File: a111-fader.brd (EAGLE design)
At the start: 100 x 50 mm, 50 parts, among them U1 FADER-KNOB-8MM(BLACK/WHITE), U10 NUT-M2-SELFLOCK, U11 FX2-20S-1.27DS, U12 ERM1-5MM, U2 SCREW-M2X8, U3 SCREW-M2X8, U4 NUT-M2-SELFLOCK, U5 NUT-M2-SELFLOCK, U6 FX2-20P-1.27DS, U7 SCREW-M2X8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

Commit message: A111 New VU Indicator preliminary
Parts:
- removed DA2: LM2903N, ic-fairchild:DIP-8
- removed R13: 22K(TH), resistors:R-0207/10
- removed R15: 100R(TH), resistors:R-0207/10
- added DA3: TL072IP, ic-ti:DIP-8
- added R20, R21: 100K(TH), resistors:R-0207/10
- added R22: 15K(TH), resistors:R-0207/10
- added R23: 470K(TH), resistors:R-0207/10
- HL1: value RED/BLUE(2MMX5MM,CC) -> RED/GREEN(2MMX5MM,CC)
- R19: value 4K7(TH) -> 10K(TH)
- R24: value 1K8(TH) -> 300K(TH)
- R25: value 10K(TH) -> 1K(TH)
- R26: value 2K2(TH) -> 1K(TH)
- R6, R8: value 10M(TH) -> 1M(TH)
- R7, R9: value 100K(TH) -> 33K(TH)
- moved C7 3.00 mm to (21.0, 39.0)
- moved C8 3.00 mm to (35.0, 39.0)
- turned R24 to 90 degrees
- renumbered R14 to R19, R16 to R25, R17 to R26, R18 to R24
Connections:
- removed net N$26: DA2.2, R15.2, R19.1
- removed net N$27: DA2.6, R13.1, R19.2
- removed net N$28: DA2.1, HL1.A2, R24.1, VT1.1
- removed net N$45: C1.+, C3.2, C7.2, DA1.8, DA2.8, L1.2
- removed net N$47: C2.-, C4.1, C8.1, DA1.4, DA2.4, L2.2
- removed net N$48: DA2.7, HL1.A1, R25.2, R26.1
- removed net N$49: R25.1, VT1.2
- new net N$13: DA3.6, R19.2, R20.1
- new net N$17: DA3.7, R20.2, R26.1
- new net N$29: HL1.A2, R26.2, VT1.1
- new net N$30: DA3.2, R21.1, R22.2, R23.2
- new net N$31: DA3.1, R21.2, R24.1, R25.1
- new net N$32: R24.2, VT1.2
- new net N$33: HL1.A1, R25.2
- net +15V: now also C1.+, C3.2, C7.2, DA1.8, DA3.8, L1.2, R23.1; no longer R13.2
- net -15V: now also C2.-, C4.1, C8.1, DA1.4, DA3.4, L2.2; no longer HL1.K, VT1.3
- net GND: now also HL1.K, R19.1, R22.1, VT1.3; no longer R15.1, R24.2, R26.2
- net N$24: now also DA3.3, DA3.5; no longer DA2.3, DA2.5
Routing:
- net N$45: track 112.4 -> 0.00 mm
- net N$47: track 92.3 -> 0.00 mm
- net N$26: track 44.5 -> 0.00 mm
- net N$24: track 61.0 -> 22.9 mm
- net -15V: track 5.96 -> 43.3 mm
- net N$27: track 33.1 -> 0.00 mm
- net N$28: track 19.8 -> 0.00 mm
- net N$48: track 18.2 -> 0.00 mm
- net N$49: track 4.07 -> 0.00 mm
- net +15V: track 44.9 -> 43.1 mm

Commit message: A111a Routing
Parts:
- removed R24: 300K(TH), resistors:R-0207/10
- removed R25: 1K(TH), resistors:R-0207/10
- added R13: 10K(TH), resistors:R-0207/10
- added R16: 100K(TH), resistors:R-0207/10
- R19: value 10K(TH) -> 1K(TH)
- R20: value 100K(TH) -> 300K(TH)
- moved R19 26.6 mm to (13.0, 40.0), turned to 90 degrees
- moved R20 22.5 mm to (5.00, 37.0), turned to 90 degrees
- renumbered DA3 to DA2, R21 to R17, R22 to R15, R23 to R14, R26 to R18
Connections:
- net GND: now also R13.1; no longer R19.1
- net N$13: now also R13.2, R16.1; no longer R19.2, R20.1
- net N$17: now also R16.2; no longer R20.2
- net N$31: now also R19.1, R20.1; no longer R24.1, R25.1
- net N$32: now also R20.2; no longer R24.2
- net N$33: now also R19.2; no longer R25.2
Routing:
- net +15V: track 43.1 -> 157.5 mm, vias 0 -> 1
- net -15V: track 43.3 -> 103.2 mm, vias 0 -> 1
- net N$30: track 0.00 -> 52.0 mm
- net N$13: track 0.00 -> 31.4 mm
- net N$24: track 22.9 -> 53.3 mm
- net N$31: track 0.00 -> 23.5 mm
- net N$17: track 0.00 -> 14.6 mm
- net N$32: track 0.00 -> 10.9 mm
- net N$29: track 0.00 -> 8.74 mm
- net N$33: track 0.00 -> 4.16 mm

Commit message: A111a: Resistor Value Update
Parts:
- R20: value 300K(TH) -> 330K(TH)
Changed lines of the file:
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@@
 <element name="R15" library="resistors" package="R-0207/10" value="15K(TH)" x="22" y="7" rot="R180"/>
 <element name="R14" library="resistors" package="R-0207/10" value="470K(TH)" x="19" y="40" rot="R90"/>
-<element name="R20" library="resistors" package="R-0207/10" value="300K(TH)" x="5" y="37" rot="R90"/>
+<element name="R20" library="resistors" package="R-0207/10" value="330K(TH)" x="5" y="37" rot="R90"/>
 <element name="R19" library="resistors" package="R-0207/10" value="1K(TH)" x="13" y="40" rot="R90">
 <attribute name="MOUSER" value="71-RN55D-F-1.0K" x="13" y="40" size="1.778" layer="27" rot="R90" display="off"/>

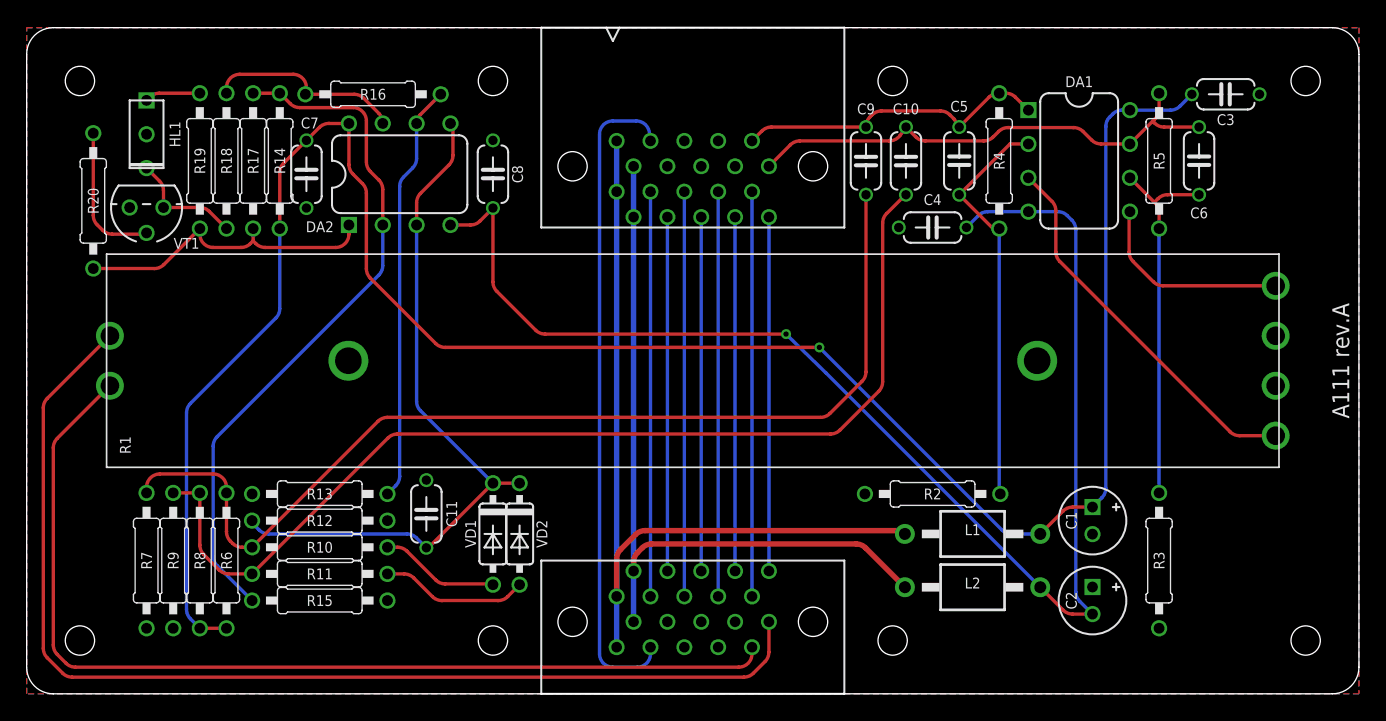
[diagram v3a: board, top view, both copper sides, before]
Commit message: A111 Change resistor positioning to better tolerate 0207 resistors
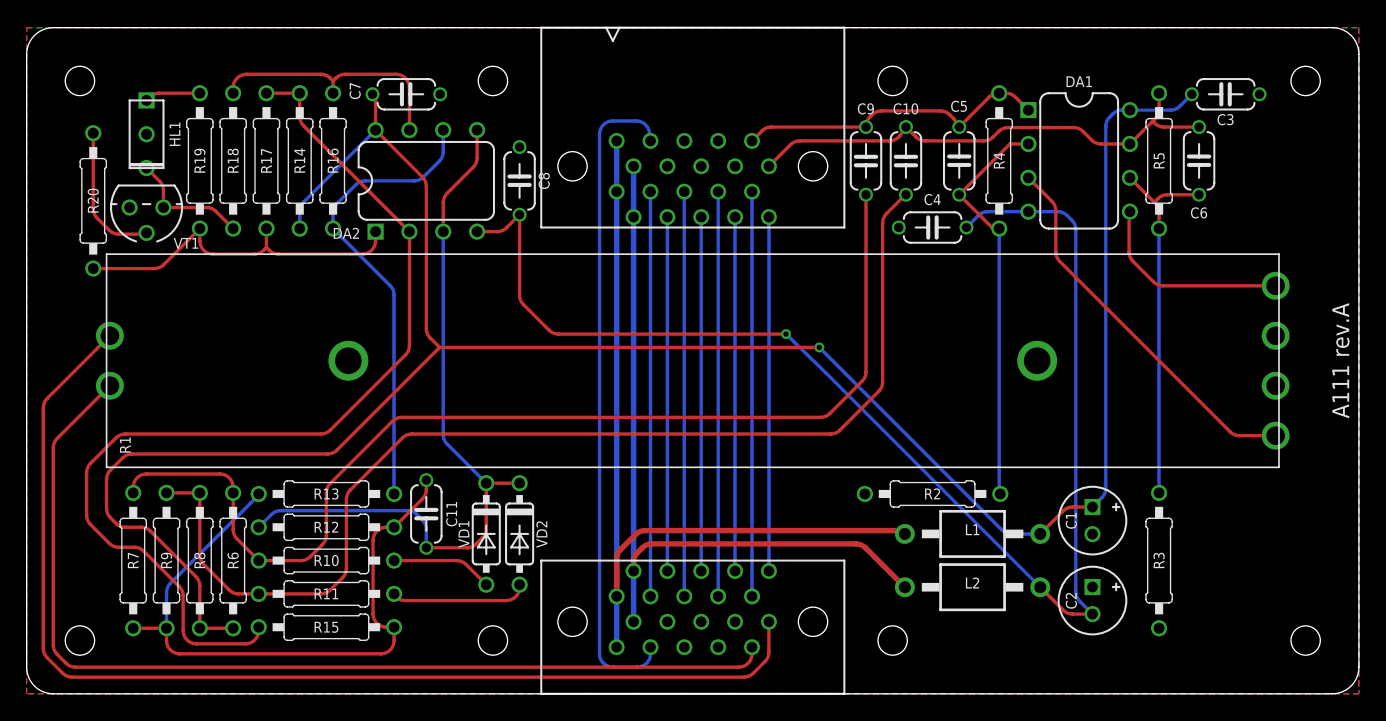
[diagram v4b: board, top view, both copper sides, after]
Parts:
- moved C7 9.60 mm to (28.5, 45.0), turned to 180 degrees
- moved R16 5.83 mm to (23.0, 40.0), turned to 90 degrees
- moved C8 2.06 mm to (37.0, 38.5)
- moved DA2 2.06 mm to (30.0, 38.5)
- moved R15 2.06 mm to (22.5, 5.00)
- moved R11 1.58 mm to (22.5, 7.50)
- moved R14 1.50 mm to (20.5, 40.0)
- moved R10 1.12 mm to (22.5, 10.0)
- moved R17 1.00 mm to (18.0, 40.0)
- moved R7 1.00 mm to (8.00, 10.0)
- moved R12 0.71 mm to (22.5, 12.5)
- moved R13 0.50 mm to (22.5, 15.0)
- moved R18 0.50 mm to (15.5, 40.0)
- moved R6 0.50 mm to (15.5, 10.0)
- moved R9 0.50 mm to (10.5, 10.0)
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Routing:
- net GND: track 0.00 -> 49.2 mm
- net N$30: track 52.0 -> 75.7 mm
- net +15V: track 157.5 -> 169.2 mm
- net N$22: track 78.9 -> 84.4 mm
- net N$17: track 14.6 -> 18.9 mm
- net N$20: track 78.0 -> 81.9 mm
- net N$13: track 31.4 -> 35.0 mm
- net N$31: track 23.5 -> 26.5 mm
- net -15V: track 103.2 -> 101.3 mm
- net N$24: track 53.3 -> 54.9 mm
- net N$21: track 8.96 -> 7.61 mm
- net N$23: track 11.1 -> 10.2 mm
- net N$29: track 8.74 -> 9.24 mm
